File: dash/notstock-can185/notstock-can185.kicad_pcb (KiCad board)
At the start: 2 copper layers, 53 x 53 mm, 27 parts, among them J1 OBD 12V GND H L, J2 LCD-1.85 header, U1 LMR16006YDDCR, U2 TJA1051T/3

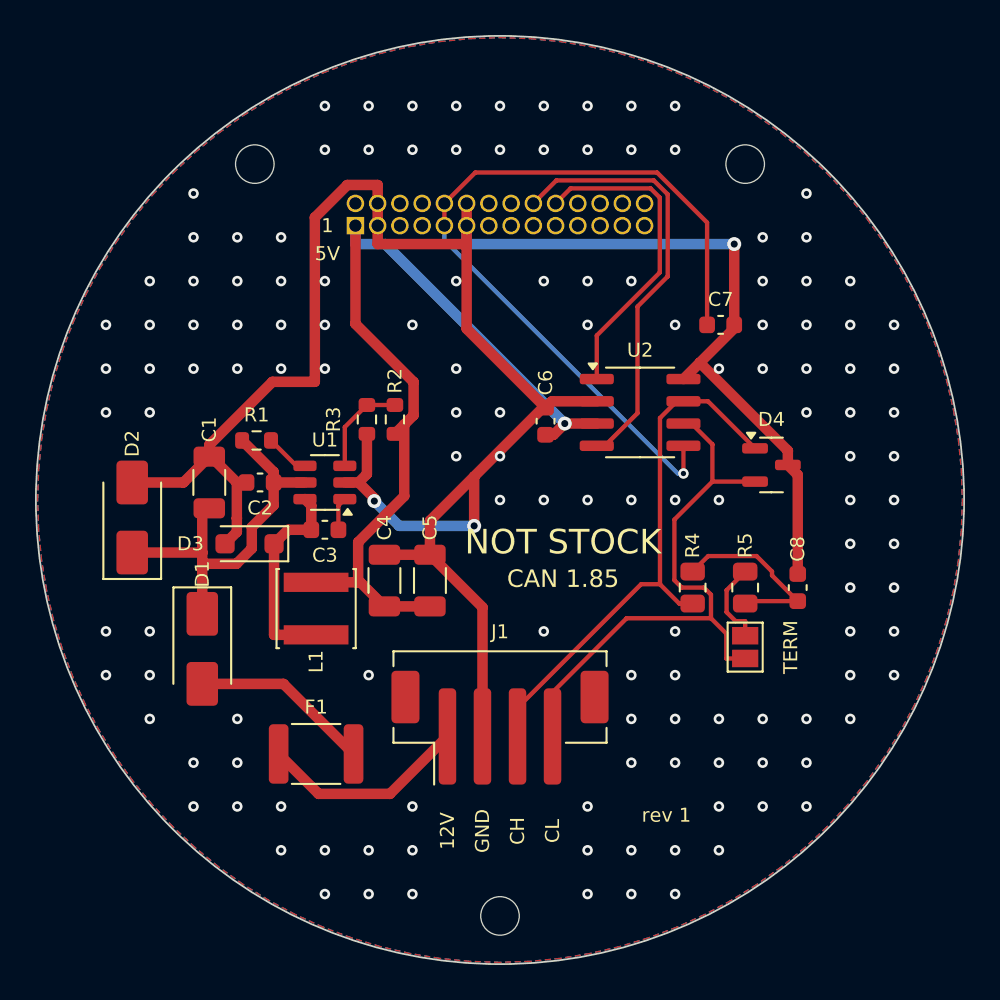
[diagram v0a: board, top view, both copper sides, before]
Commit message: CAN 1.85 rev 2: the real ESP32-S3-Touch-LCD-1.85's mechanics and sockets
Waveshare's drawing and schematic of the board (ESP32-S3-LCD-1.85) show
no plug-on header: rev 1 followed the 1.85C, which has one. Now:
Ø48 outline and the three M2 holes from the drawing (DXF), CAN through the
display's 4-pin 1.0 mm UART socket on a 1:1 JST SH cable (GPIO44 TX,
GPIO43 RX, 3V3, GND; 1 k in RXD against the boot ROM's output on
GPIO43), 5 V to the display's USB-C from a USB-C socket on this board.
Edge keepout for the autorouter. DRC clean.

Firmware for the 1.85: CAN on GPIO44/43, the boot loader quiet; the
touch's GPIO1/3 noted as this board's.

Co-Authored-By: Claude Opus 5.5 <noreply@anthropic.com>
Claude-Session: https://claude.ai/code/session_018SKN4tJhAPpVCWtvRZgZpD
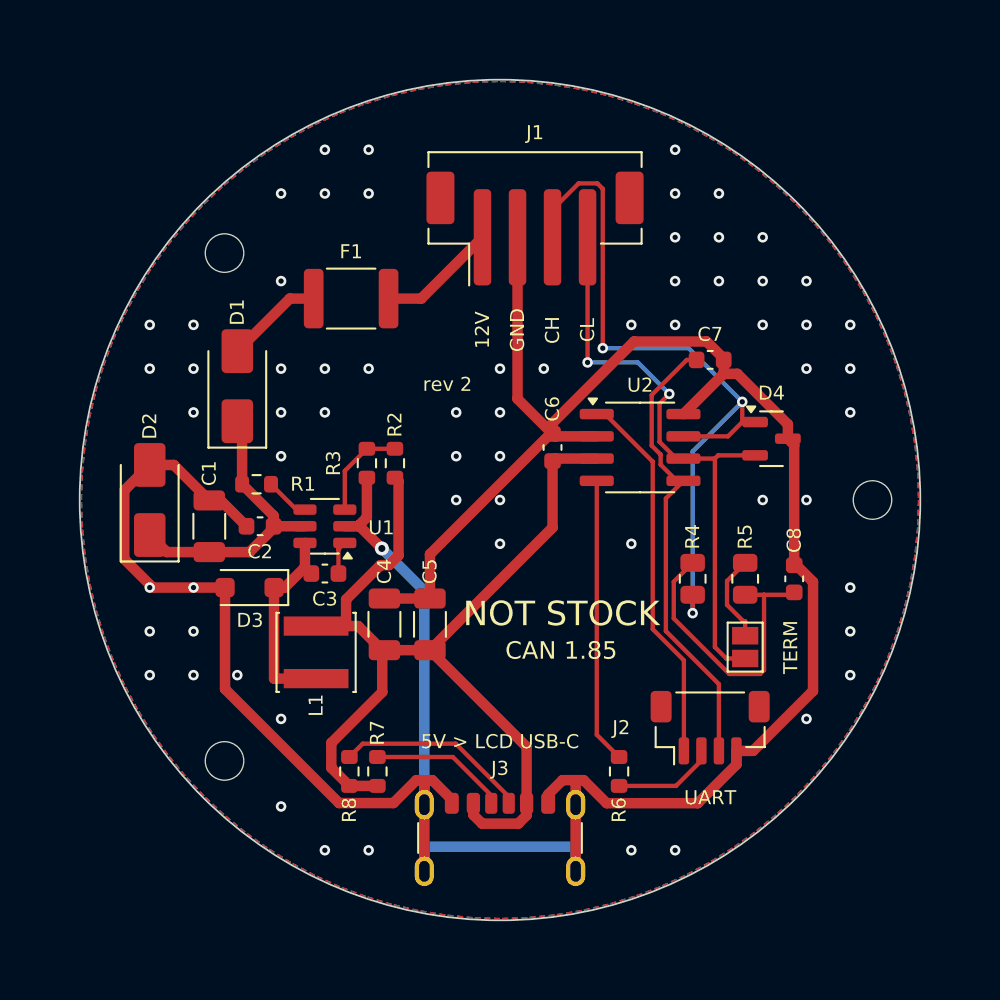
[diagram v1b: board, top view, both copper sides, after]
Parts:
- added J3: 5V to display, Connector_USB:USB_C_Receptacle_GCT_USB4125-xx-x_6P_TopMnt_Horizontal, F.Cu at (150.0, 120.4)
- added R6: 1k, Resistor_SMD:R_0603_1608Metric, F.Cu at (156.8, 115.5)
- added R7: 56k, Resistor_SMD:R_0603_1608Metric, F.Cu at (143.0, 115.5)
- added R8: 56k, Resistor_SMD:R_0603_1608Metric, F.Cu at (141.4, 115.5)
- J2: value LCD-1.85 header -> to display UART; footprint Connector_PinSocket_1.27mm:PinSocket_2x14_P1.27mm_Vertical -> Connector_JST:JST_SH_BM04B-SRSS-TB_1x04-1MP_P1.00mm_Vertical; moved to F.Cu
- moved H2 45.2 mm to (134.3, 114.9)
- moved J2 35.1 mm to (162.0, 113.0), turned to 0 degrees
- moved H3 31.9 mm to (171.3, 100.0)
- moved J1 28.6 mm to (152.0, 84.5)
- moved F1 26.1 mm to (141.5, 88.5), turned to 180 degrees
- moved D1 15.1 mm to (135.0, 93.5), turned to 90 degrees
- moved H1 5.37 mm to (134.3, 85.9)
- moved C1 2.50 mm to (133.4, 101.5)
- moved C2 2.50 mm to (136.3, 101.5)
- moved C3 2.50 mm to (140.0, 104.2)
- moved C4 2.50 mm to (143.4, 107.1)
- moved C5 2.50 mm to (146.0, 107.1)
- moved D3 2.50 mm to (135.7, 105.0)
- moved L1 2.50 mm to (139.5, 108.7)
- moved R1 2.50 mm to (136.1, 99.1)
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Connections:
- J2 pad 1: +5V -> TXD
- J2 pad 2: (no net) -> RXD
- J2 pad 3: GND -> +3V3
- U2 pad 4: RXD -> RXD_T
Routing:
- net GND: track 137.8 -> 171.9 mm, vias 138 -> 65
- net +3V3: track 45.6 -> 26.4 mm, vias 1 -> 0
- net RXD: track 24.9 -> 5.85 mm
- net RXD_T: track 0.00 -> 16.3 mm
- net CANH: track 31.4 -> 43.4 mm, vias 0 -> 3
- net CC2: track 0.00 -> 11.0 mm
- net +5V: track 51.3 -> 60.2 mm, vias 1 -> 0
- net CC1: track 0.00 -> 7.86 mm
- net TMID: track 10.6 -> 17.3 mm
- net VIN: track 22.6 -> 16.8 mm
- net VBAT: track 11.9 -> 6.81 mm
- net VBAT_F: track 10.3 -> 5.61 mm
- net TXD: track 18.4 -> 21.6 mm
- net CANL: track 34.1 -> 34.2 mm, vias 0 -> 2
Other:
- board size 53 x 53 mm -> 48 x 48 mm
- board text added: "5V > LCD USB-C"
- board text added: "UART"
- board text added: "rev 2"
- board text removed: "1"
- board text removed: "5V"
- board text removed: "LCD SIDE"
- board text removed: "rev 1"

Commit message: CAN 1.85 rev 3: ready for JLCPCB assembly
LCSC numbers for every part (looked up on LCSC/JLCPCB), in design.py,
the schematic (LCSC and MPN fields), the footprints and fab/bom.csv;
values matched to the parts (22 uF 16 V). J3 now the HRO TYPE-C-31-M-12
JLCPCB stocks; its two VBUS pad pairs joined by a short bridge
underneath before autorouting (and routes coming back from the session
not duplicated). Silkscreen past the edge trimmed. DRC clean.

Co-Authored-By: Claude Opus 5.5 <noreply@anthropic.com>
Claude-Session: https://claude.ai/code/session_018SKN4tJhAPpVCWtvRZgZpD
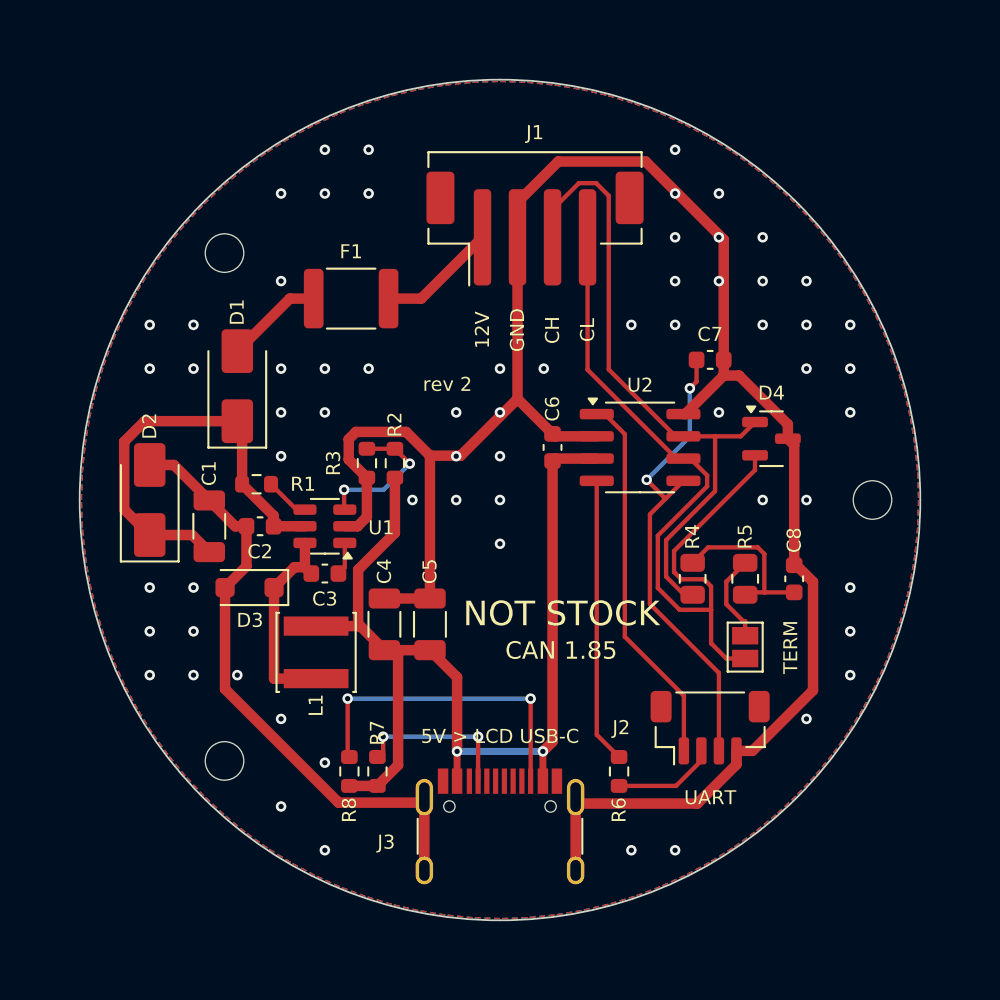
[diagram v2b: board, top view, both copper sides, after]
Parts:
- C4, C5: value 22u 10V -> 22u 16V
- J3: footprint Connector_USB:USB_C_Receptacle_GCT_USB4125-xx-x_6P_TopMnt_Horizontal -> Connector_USB:USB_C_Receptacle_HRO_TYPE-C-31-M-12
- moved J3 0.30 mm to (150.0, 120.1)
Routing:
- net GND: track 171.9 -> 147.6 mm, vias 65 -> 64
- net CANL: track 34.2 -> 44.6 mm, vias 2 -> 0
- net VIN: track 16.8 -> 25.3 mm
- net TMID: track 17.3 -> 9.66 mm
- net CC2: track 11.0 -> 18.5 mm, vias 0 -> 2
- net CANH: track 43.4 -> 37.0 mm, vias 3 -> 0
- net FB: track 5.60 -> 8.31 mm, vias 0 -> 2
- net CC1: track 7.86 -> 9.25 mm, vias 0 -> 2
- net +3V3: track 26.4 -> 27.4 mm, vias 0 -> 2
- net +5V: track 60.2 -> 60.4 mm, vias 0 -> 2

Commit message: CAN 1.85: R4/R5 62 R Walsin C5805111 (60.4 R out of stock)
Co-Authored-By: Claude Opus 5.5 <noreply@anthropic.com>
Claude-Session: https://claude.ai/code/session_018SKN4tJhAPpVCWtvRZgZpD
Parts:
- R4, R5: value 60R4 -> 62R
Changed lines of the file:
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@@
     (descr "Resistor SMD 0805 (2012 Metric), square (rectangular) end terminal, IPC_7351 nominal, (Body size source: IPC-SM-782 page 72, https://www.pcb-3d.com/wordpress/wp-content/uploads/ipc-sm-782a_amendment_1_and_2.pdf), generated with kicad-footprint-generator")
     (tags "resistor")
-    (property "LCSC" "C273897")
+    (property "LCSC" "C5805111")
     (attr smd)
     (fp_text reference "R4" (at 2.405 0 90) (layer "F.SilkS")
         (effects (font (size 0.8 0.8) (thickness 0.13)))
     )
-    (fp_text value "60R4" (at 0 1.65 90) (layer "F.Fab") hide
+    (fp_text value "62R" (at 0 1.65 90) (layer "F.Fab") hide
         (effects (font (size 1 1) (thickness 0.15)))
     )
@@
     (descr "Resistor SMD 0805 (2012 Metric), square (rectangular) end terminal, IPC_7351 nominal, (Body size source: IPC-SM-782 page 72, https://www.pcb-3d.com/wordpress/wp-content/uploads/ipc-sm-782a_amendment_1_and_2.pdf), generated with kicad-footprint-generator")
     (tags "resistor")
-    (property "LCSC" "C273897")
+    (property "LCSC" "C5805111")
     (attr smd)
     (fp_text reference "R5" (at 2.405 0 90) (layer "F.SilkS")
         (effects (font (size 0.8 0.8) (thickness 0.13)))
     )
-    (fp_text value "60R4" (at 0 1.65 90) (layer "F.Fab") hide
-        (effects (font (size 1 1) (thickness 0.15)))
-    )
+    (fp_text value "62R" (at 0 1.65 90) (layer "F.Fab") hide
+        (effects (font (size 1 1) (thickness 0.15)))
+    )

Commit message: CAN 1.85 rev 4: power the display through its battery socket
12 V -> 3.75 V into the display's battery input on two wires instead of
5 V into its USB-C (no room for a cable). USB-C, CC resistors gone;
SN65HVD230 on the display's 3.3 V replaces the 5 V TJA1051T/3. The
display's Key1 must be bridged so its battery switch turns on.

Co-Authored-By: Claude Opus 5.5 <noreply@anthropic.com>
Claude-Session: https://claude.ai/code/session_018SKN4tJhAPpVCWtvRZgZpD
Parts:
- removed R7, R8: 56k, Resistor_SMD:R_0603_1608Metric
- J3: value 5V to display -> BAT to display; footprint Connector_USB:USB_C_Receptacle_HRO_TYPE-C-31-M-12 -> Connector_Wire:SolderWire-0.25sqmm_1x02_P4.2mm_D0.65mm_OD1.7mm
- R2: value 56k -> 39k
- U2: value TJA1051T/3 -> SN65HVD230
- moved J3 1.10 mm to (150.0, 119.0)
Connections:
- C4 pad 1: +5V -> BAT_LCD
- C5 pad 1: +5V -> BAT_LCD
- C6 pad 1: +5V -> +3V3
- L1 pad 2: +5V -> BAT_LCD
- R2 pad 1: +5V -> BAT_LCD
- U2 pad 3: +5V -> +3V3
- U2 pad 5: +3V3 -> (no net)
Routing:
- net +5V: track 60.4 -> 0.00 mm, vias 2 -> 0
- net BAT_LCD: track 0.00 -> 29.8 mm
- net CC2: track 18.5 -> 0.00 mm, vias 2 -> 0
- net +3V3: track 27.4 -> 41.5 mm
- net CANH: track 37.0 -> 49.7 mm
- net CANL: track 44.6 -> 32.0 mm
- net CC1: track 9.25 -> 0.00 mm, vias 2 -> 0
- net GND: track 147.6 -> 155.1 mm, vias 64 -> 76
- net TMID: track 9.66 -> 16.4 mm
- net FB: track 8.31 -> 5.60 mm, vias 2 -> 0
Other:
- board text added: "+"
- board text added: "-"
- board text added: "3V75 > LCD BAT"
- board text added: "rev 4"
- board text removed: "5V > LCD USB-C"
- board text removed: "rev 2"

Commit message: CAN 1.85 rev 4: UART cable soldered to pads instead of an SH socket
The display comes with a cable plugged into its UART socket; its free
ends are soldered to J2 now, marked with the display's names. J3 labels
moved onto its pads. R6 moved for the labels.

Co-Authored-By: Claude Opus 5.5 <noreply@anthropic.com>
Claude-Session: https://claude.ai/code/session_018SKN4tJhAPpVCWtvRZgZpD
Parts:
- J2: value to display UART -> UART wires from display; footprint Connector_JST:JST_SH_BM04B-SRSS-TB_1x04-1MP_P1.00mm_Vertical -> Connector_Wire:SolderWire-0.15sqmm_1x04_P4mm_D0.5mm_OD1.5mm
- moved J2 6.08 mm to (156.0, 112.0)
- moved J3 2.10 mm to (147.9, 119.0)
- moved R6 1.77 mm to (155.6, 116.8)
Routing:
- net CANL: track 32.0 -> 54.2 mm
- net CANH: track 49.7 -> 30.2 mm
- net +3V3: track 41.5 -> 60.6 mm, vias 2 -> 1
- net GND: track 155.1 -> 143.9 mm, vias 76 -> 74
- net TMID: track 16.4 -> 9.59 mm
- net FB: track 5.60 -> 9.15 mm, vias 0 -> 2
- net TXD: track 21.6 -> 18.5 mm
- net BAT_LCD: track 29.8 -> 27.6 mm
- net RXD_T: track 16.3 -> 18.1 mm
- net RXD: track 5.84 -> 7.45 mm
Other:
- board text added: "3V3"
- board text added: "IO43"
- board text added: "IO44"
- board text added: "UART from LCD"
- board text removed: "UART"

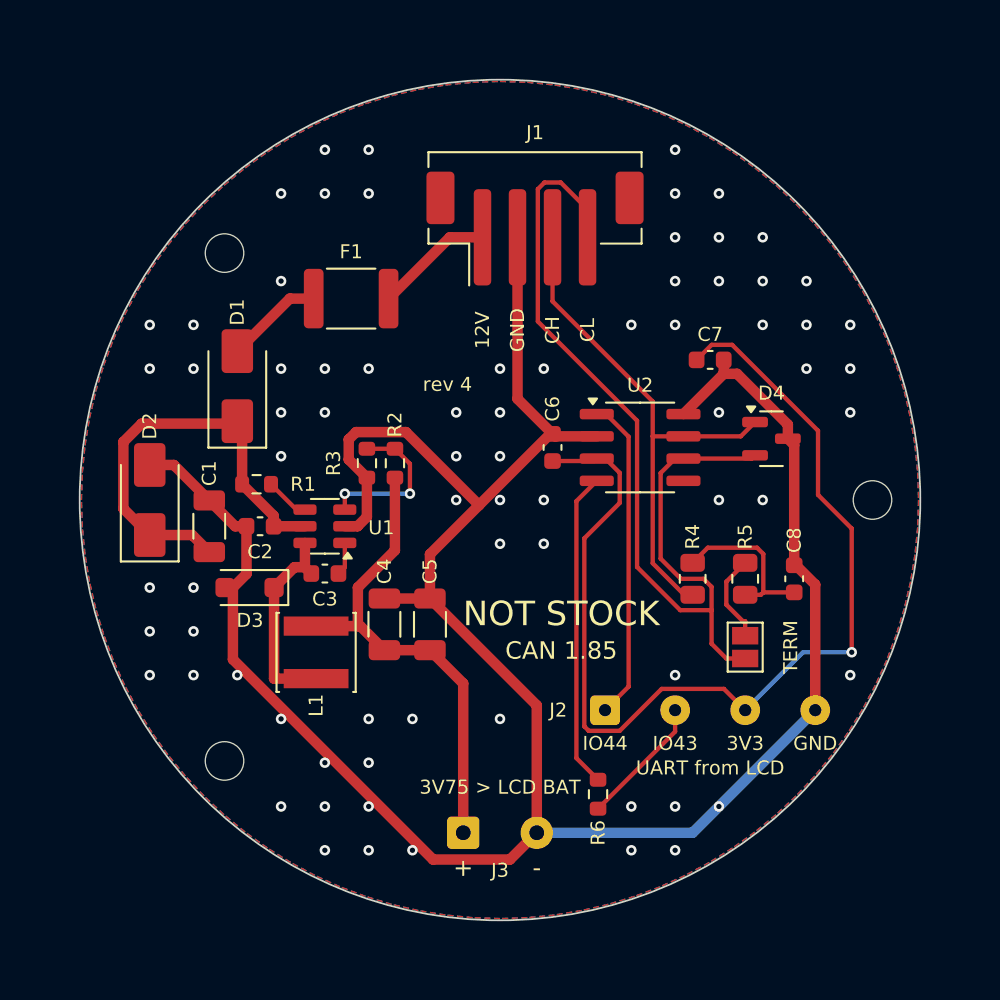
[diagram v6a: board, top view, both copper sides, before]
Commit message: CAN 1.85 rev 5: on and off with the key through the K-line
OBD pin 7 onto the regulator's EN through 100 k / 13 k (on above 10.5 V,
off below 9.3 V), 100 nF against K-line traffic. J1 becomes a 5-pin JST PH,
vertical.

Co-Authored-By: Claude Opus 5.5 <noreply@anthropic.com>
Claude-Session: https://claude.ai/code/session_018SKN4tJhAPpVCWtvRZgZpD
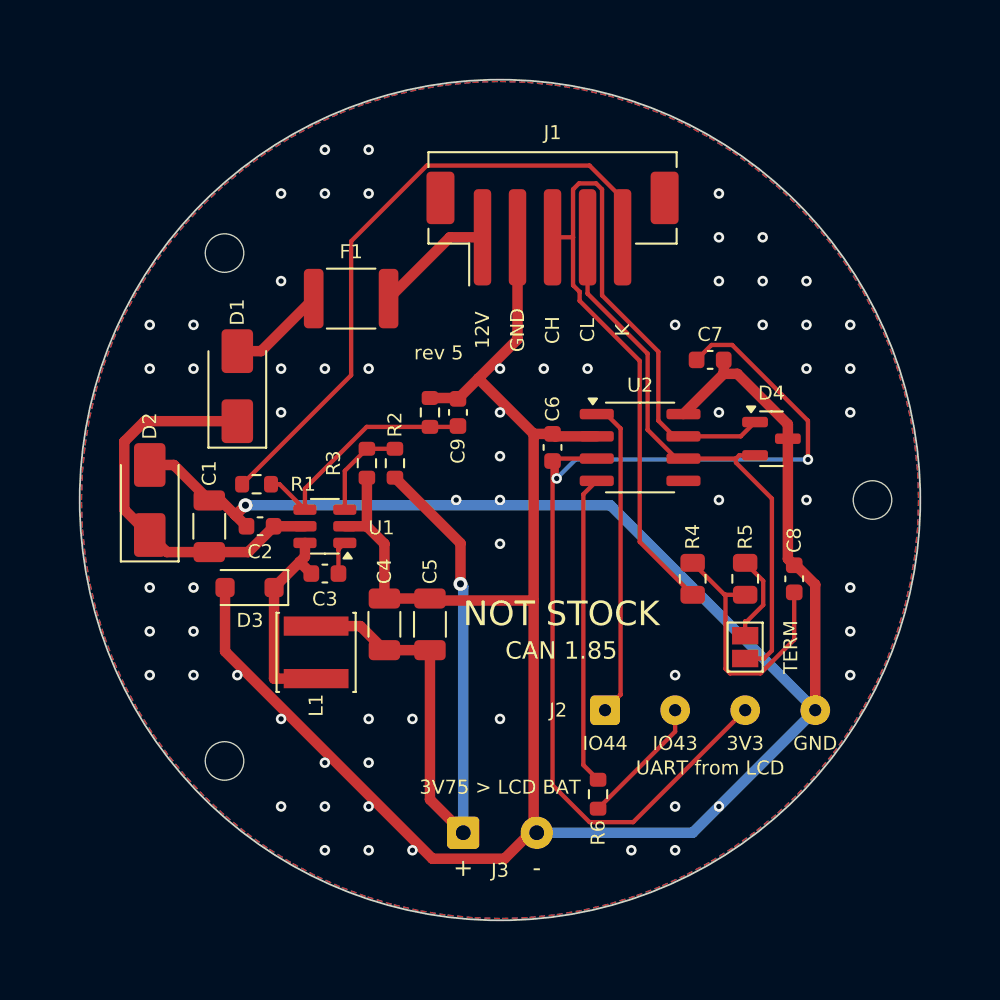
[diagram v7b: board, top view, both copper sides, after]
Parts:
- added C9: 100n, Capacitor_SMD:C_0603_1608Metric, F.Cu at (147.6, 95.0)
- added R9: 13k, Resistor_SMD:R_0603_1608Metric, F.Cu at (146.0, 95.0)
- J1: value OBD 12V GND H L -> OBD 12V GND H L K; footprint Connector_JST:JST_PH_B4B-PH-SM4-TB_1x04-1MP_P2.00mm_Vertical -> Connector_JST:JST_PH_B5B-PH-SM4-TB_1x05-1MP_P2.00mm_Vertical
- moved J1 1.00 mm to (153.0, 84.5)
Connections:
- R1 pad 1: VIN -> KLINE
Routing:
- net KLINE: track 0.00 -> 36.7 mm
- net GND: track 143.9 -> 177.1 mm, vias 74 -> 66
- net CANL: track 54.2 -> 32.8 mm
- net CANH: track 30.2 -> 49.9 mm
- net BAT_LCD: track 27.6 -> 40.2 mm, vias 0 -> 1
- net EN: track 2.54 -> 14.0 mm
- net TMID: track 9.59 -> 15.5 mm
- net FB: track 9.15 -> 5.60 mm, vias 2 -> 0
- net VIN: track 25.3 -> 22.8 mm
- net +3V3: track 60.6 -> 62.1 mm, vias 1 -> 2
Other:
- board text added: "K"
- board text added: "rev 5"
- board text removed: "rev 4"

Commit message: CAN 1.85 rev 5: ignition from OBD pin 1 (terminal 15) instead of the K-line
VW puts terminal 15 on OBD pin 1, as the CANcheck display uses it. Same
divider onto EN; J1 pin 5 marked 15.

Co-Authored-By: Claude Opus 5.5 <noreply@anthropic.com>
Claude-Session: https://claude.ai/code/session_018SKN4tJhAPpVCWtvRZgZpD
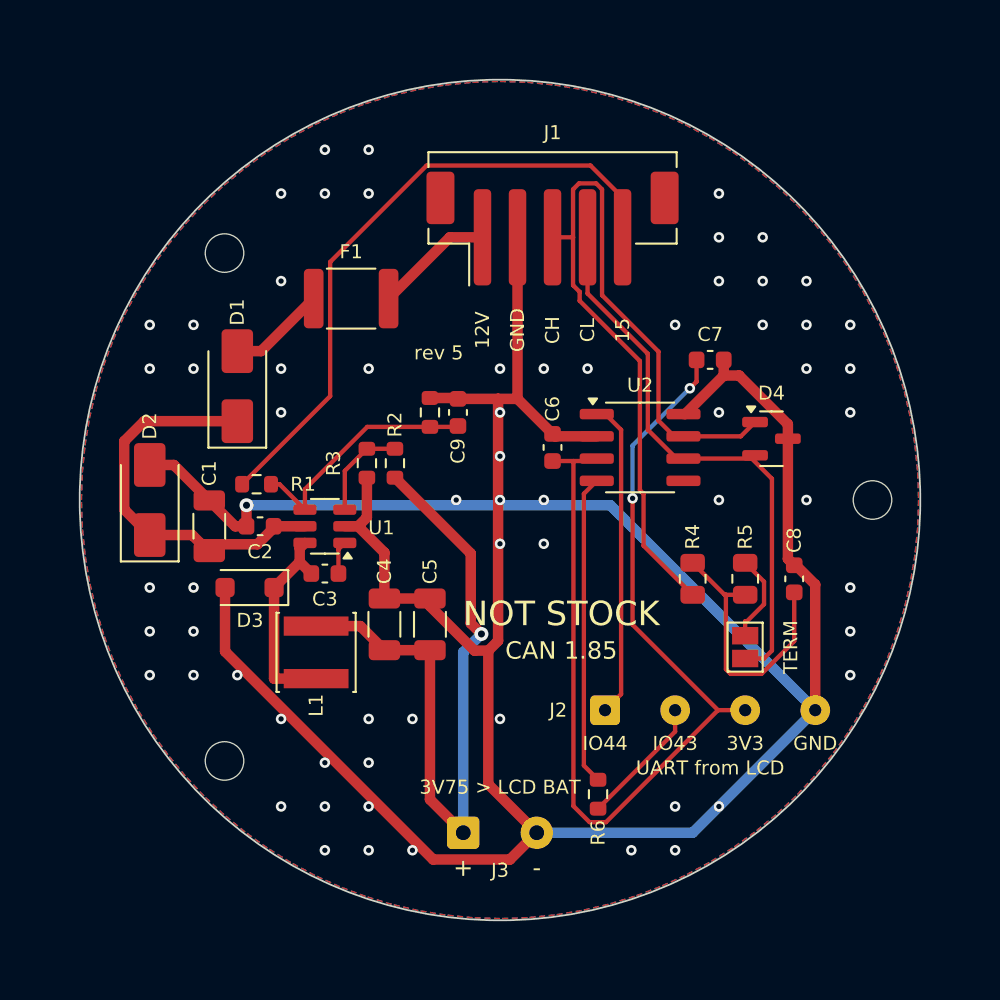
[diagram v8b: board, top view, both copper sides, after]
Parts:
- J1: value OBD 12V GND H L K -> OBD 12V GND H L 15
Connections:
- net KLINE renamed IGN
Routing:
- net +3V3: track 62.1 -> 58.7 mm
- net GND: track 177.1 -> 179.0 mm
- net BAT_LCD: track 40.2 -> 41.0 mm
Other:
- board text added: "15"
- board text removed: "K"
